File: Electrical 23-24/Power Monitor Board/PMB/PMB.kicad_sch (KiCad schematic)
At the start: 11 parts, among them J1 Conn_01x03_Pin

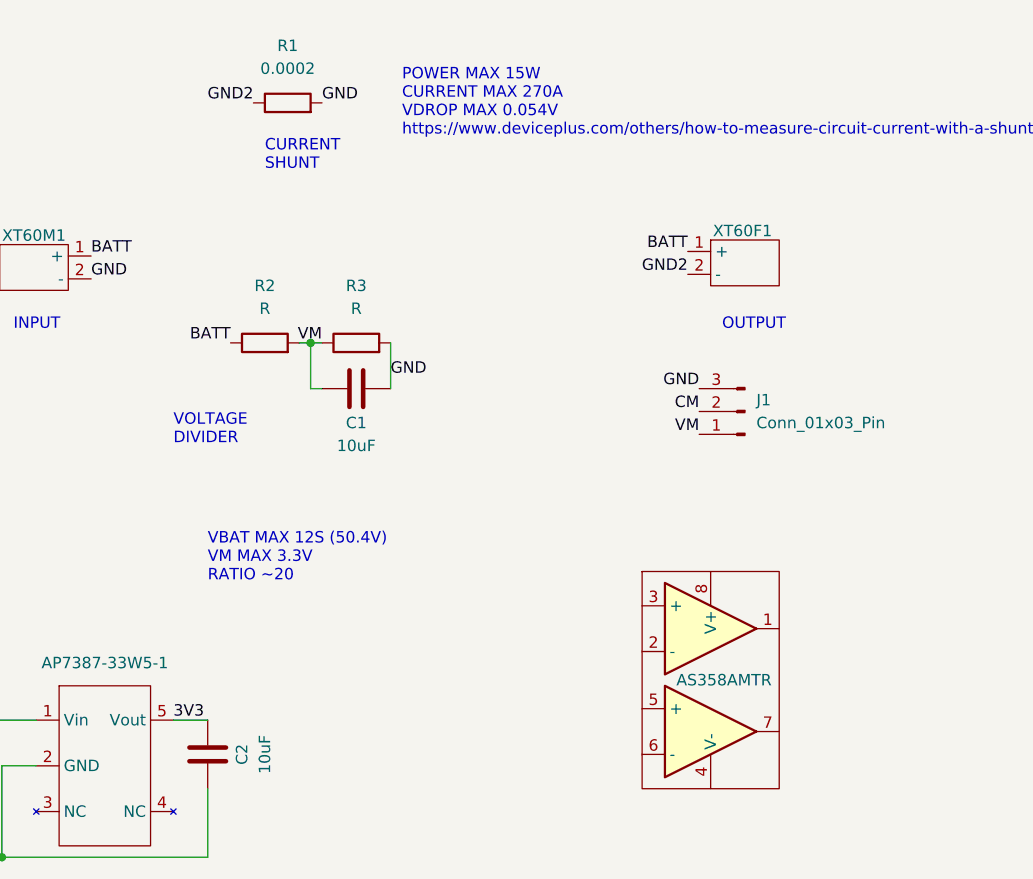
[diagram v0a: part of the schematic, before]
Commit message: Finish schematic
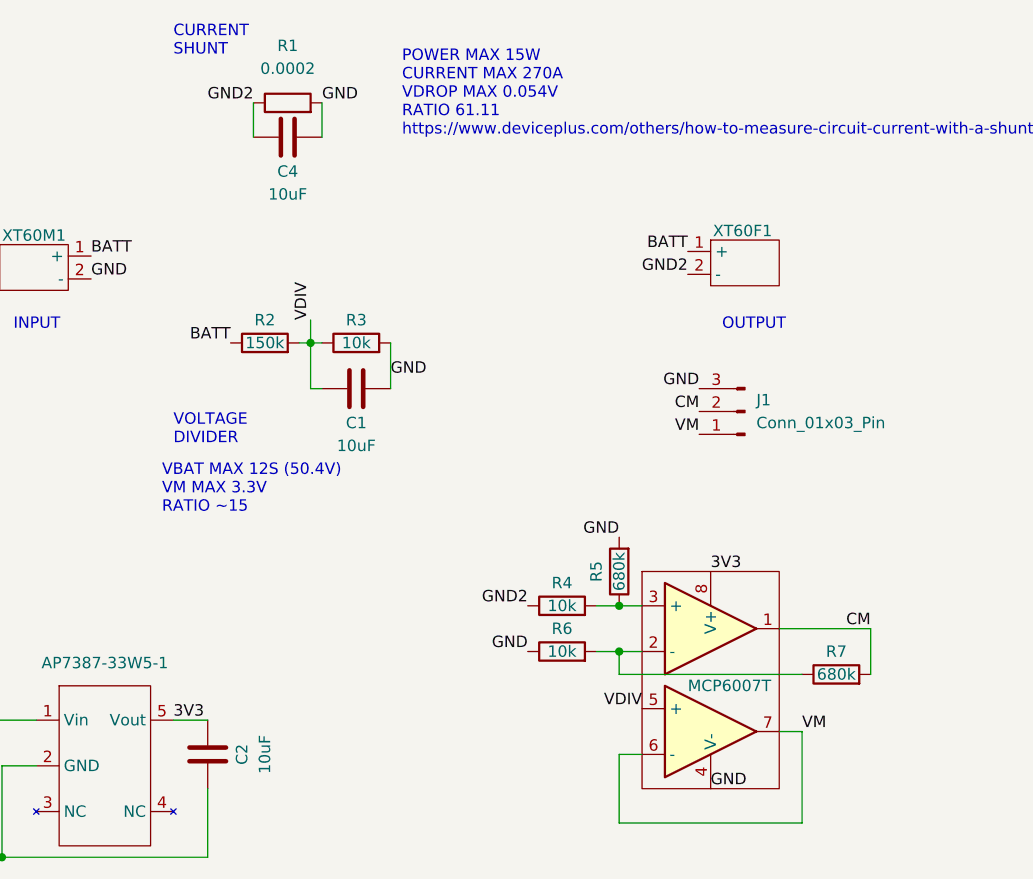
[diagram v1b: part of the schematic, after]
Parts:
- added C4: 10uF, Capacitor_SMD:C_0603_1608Metric_Pad1.08x0.95mm_HandSolder, symbol Device:C
- added R4, R6: 10k, symbol Device:R
- added R5, R7: 680k, symbol Device:R
- C1: footprint (none) -> Capacitor_SMD:C_0603_1608Metric_Pad1.08x0.95mm_HandSolder
- J1: footprint (none) -> Connector_JST:JST_XH_S3B-XH-A_1x03_P2.50mm_Horizontal
- MCP6007T: renamed from AS358AMTR; symbol PMB:AS358 -> PMB:MCP6007T-E/MS; Digi (none) -> https://www.digikey.com/en/products/detail/microchip-techno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; Num (none) -> MCP6007T-E/MS
- R1: footprint (none) -> PMB:6030_15075Metric_Pad4.20x7.60mm_HandSolder
- R2: value R -> 150k; footprint (none) -> Resistor_SMD:R_0603_1608Metric_Pad0.98x0.95mm_HandSolder
- R3: value R -> 10k; footprint (none) -> Resistor_SMD:R_0603_1608Metric_Pad0.98x0.95mm_HandSolder
- XT60F1: footprint (none) -> Connector_AMASS:AMASS_XT60PW-F_1x02_P7.20mm_Horizontal
- XT60M1: footprint (none) -> Connector_AMASS:AMASS_XT60PW-M_1x02_P7.20mm_Horizontal
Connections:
- net 3V3: now also MCP6007T.8 (V+)
- net CM: now also MCP6007T.1, R7.2
- net GND: now also MCP6007T.4 (V-), C4.2, R5.2, R6.1
- net GND2: now also C4.1, R4.1
- net VM: now also MCP6007T.6 (-), MCP6007T.7; no longer C1.1, R2.2, R3.1
- net at MCP6007T.2 (-): now also R6.2, R7.1
- net at MCP6007T.3 (+): now also R4.2, R5.1
- net VDIV: now reaches MCP6007T.5 (+)
- net VDIV: now also C1.1, R2.2, R3.1
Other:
- note added: "POWER MAX 15W CURRENT MAX 270A VDROP MAX 0.054V RATIO 61.11 https://www.deviceplus.com/others/how-to-measure-circuit-current-with-a-shunt-resistor/"
- note added: "VBAT MAX 12S (50.4V) VM MAX 3.3V RATIO ~15"
- note removed: "POWER MAX 15W CURRENT MAX 270A VDROP MAX 0.054V https://www.deviceplus.com/others/how-to-measure-circuit-current-with-a-shunt-resistor/"
- note removed: "VBAT MAX 12S (50.4V) VM MAX 3.3V RATIO ~20"

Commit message: Add all footprints
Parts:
- AP7387-33W5-1: footprint (none) -> Package_TO_SOT_SMD:SOT-23-5_HandSoldering
- C2, C3: footprint (none) -> Capacitor_SMD:C_0603_1608Metric_Pad1.08x0.95mm_HandSolder
- MCP6007T: footprint (none) -> Package_SO:TSSOP-8_4.4x3mm_P0.65mm
- R4, R5, R6, R7: footprint (none) -> Resistor_SMD:R_0603_1608Metric_Pad0.98x0.95mm_HandSolder
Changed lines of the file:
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@@
       (effects (font (size 1.27 1.27)))
     )
-    (property "Footprint" "" (at 149.86 121.92 0)
+    (property "Footprint" "Package_SO:TSSOP-8_4.4x3mm_P0.65mm" (at 149.86 121.92 0)
       (effects (font (size 1.27 1.27)) hide)
     )
@@
       (effects (font (size 1.27 1.27)))
     )
-    (property "Footprint" "" (at 94.2848 132.08 0)
+    (property "Footprint" "Capacitor_SMD:C_0603_1608Metric_Pad1.08x0.95mm_HandSolder" (at 94.2848 132.08 0)
       (effects (font (size 1.27 1.27)) hide)
     )
@@
       (effects (font (size 1.27 1.27)))
     )
-    (property "Footprint" "" (at 142.748 115.57 90)
+    (property "Footprint" "Resistor_SMD:R_0603_1608Metric_Pad0.98x0.95mm_HandSolder" (at 142.748 115.57 90)
       (effects (font (size 1.27 1.27)) hide)
     )
@@
       (effects (font (size 1.27 1.27)))
     )
-    (property "Footprint" "" (at 134.62 126.238 90)
+    (property "Footprint" "Resistor_SMD:R_0603_1608Metric_Pad0.98x0.95mm_HandSolder" (at 134.62 126.238 90)
       (effects (font (size 1.27 1.27)) hide)
     )
@@
       (effects (font (size 1.27 1.27)))
     )
-    (property "Footprint" "" (at 165.1 128.778 90)
+    (property "Footprint" "Resistor_SMD:R_0603_1608Metric_Pad0.98x0.95mm_HandSolder" (at 165.1 128.778 90)
       (effects (font (size 1.27 1.27)) hide)
     )
@@
       (effects (font (size 1.27 1.27)))
     )
-    (property "Footprint" "" (at 68.2752 139.7 0)
+    (property "Footprint" "Capacitor_SMD:C_0603_1608Metric_Pad1.08x0.95mm_HandSolder" (at 68.2752 139.7 0)
       (effects (font (size 1.27 1.27)) hide)
     )
@@
       (effects (font (size 1.27 1.27)))
     )
-    (property "Footprint" "" (at 83.82 137.16 0)
+    (property "Footprint" "Package_TO_SOT_SMD:SOT-23-5_HandSoldering" (at 83.82 137.16 0)
       (effects (font (size 1.27 1.27)) hide)
     )
@@
       (effects (font (size 1.27 1.27)))
     )
-    (property "Footprint" "" (at 134.62 121.158 90)
-      (effects (font (size 1.27 1.27)) hide)
-    )
+    (property "Footprint" "Resistor_SMD:R_0603_1608Metric_Pad0.98x0.95mm_HandSolder" (at 134.62 121.158 90)
+      (effects (font (size 1.27 1.27)) hide)
+    )

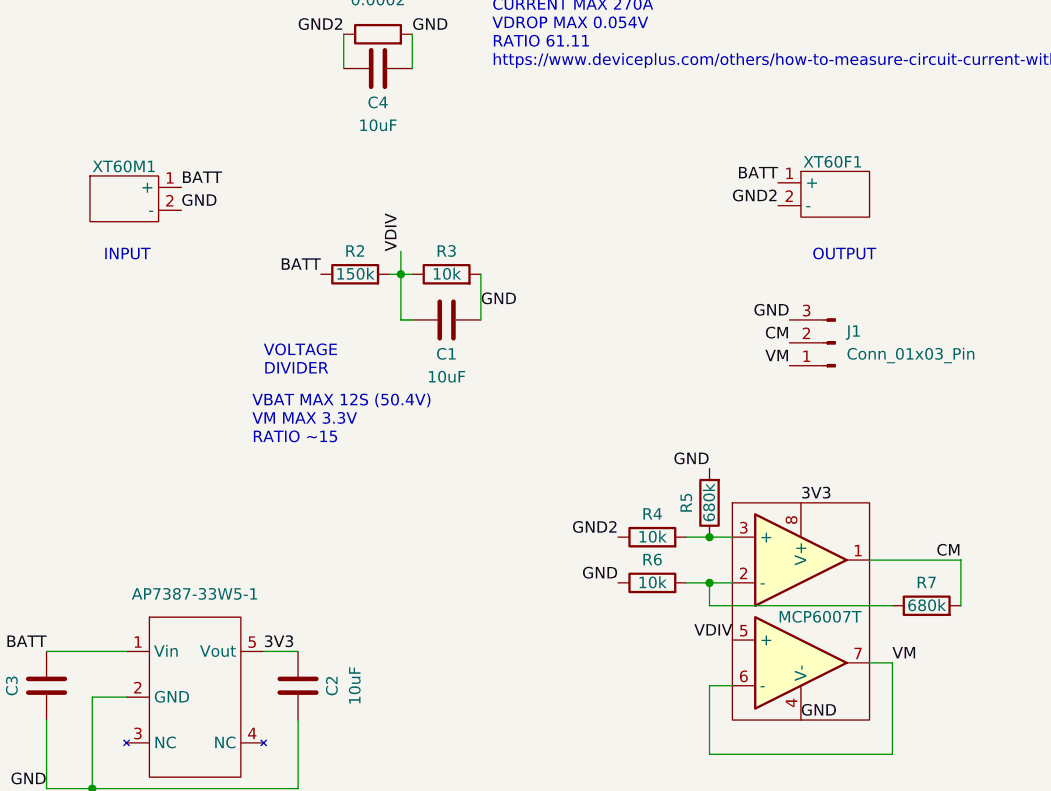
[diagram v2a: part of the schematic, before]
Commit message: Started layout
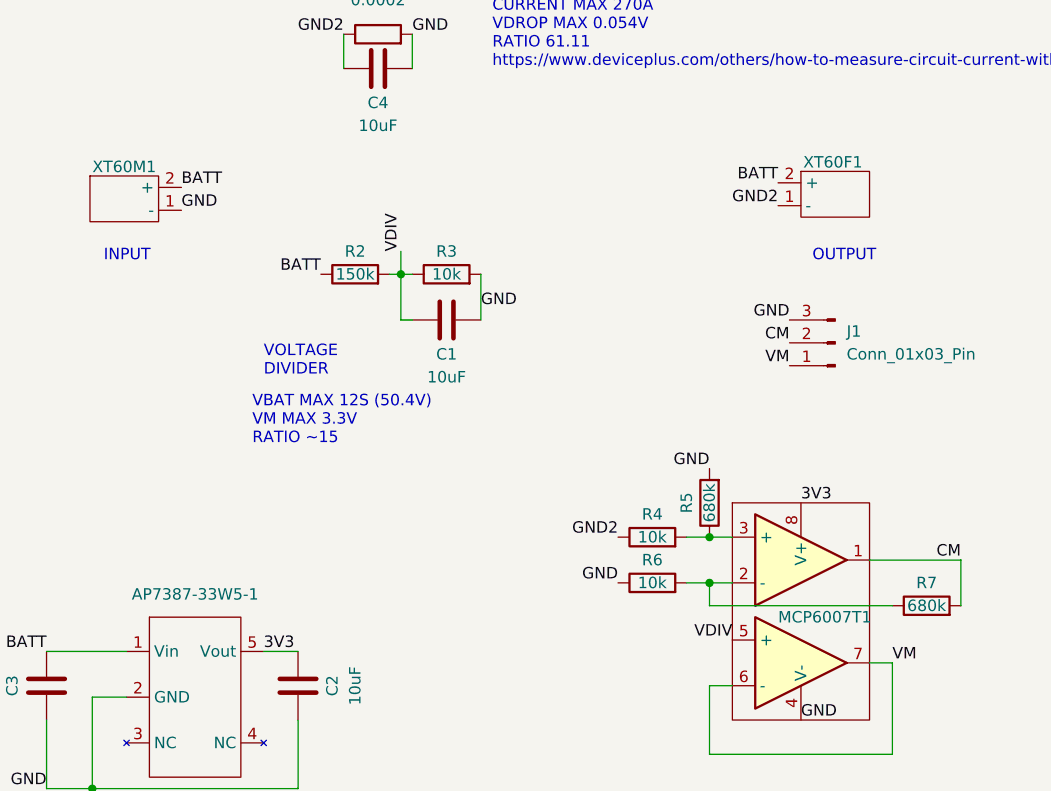
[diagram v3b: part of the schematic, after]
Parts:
- MCP6007T1: renamed from MCP6007T; footprint Package_SO:TSSOP-8_4.4x3mm_P0.65mm -> Package_SO:TSSOP-8_3x3mm_P0.65mm
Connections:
- net BATT: now also XT60F1.2 (+), XT60M1.2 (+); no longer XT60F1.1 (+), XT60M1.1 (+)
- net GND: now also XT60M1.1 (-); no longer XT60M1.2 (-)
- net GND2: now also XT60F1.1 (-); no longer XT60F1.2 (-)
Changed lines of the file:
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@@
   (symbol (lib_id "PMB:MCP6007T-E/MS") (at 149.86 121.92 0) (unit 1)
     (in_bom yes) (on_board yes) (dnp no)
-    (property "Reference" "MCP6007T" (at 148.59 128.27 0)
+    (property "Reference" "MCP6007T1" (at 148.59 128.27 0)
       (effects (font (size 1.27 1.27)) (justify left))
     )
@@
       (effects (font (size 1.27 1.27)))
     )
-    (property "Footprint" "Package_SO:TSSOP-8_4.4x3mm_P0.65mm" (at 149.86 121.92 0)
+    (property "Footprint" "Package_SO:TSSOP-8_3x3mm_P0.65mm" (at 149.86 121.92 0)
       (effects (font (size 1.27 1.27)) hide)
     )
@@
       (project "PMB"
         (path "/9d1f1551-ce55-43c8-b593-2802df254ad7"
-          (reference "MCP6007T") (unit 1)
+          (reference "MCP6007T1") (unit 1)
         )
       )

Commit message: Finish PMB
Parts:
- BATT1: renamed from XT60M1; footprint Connector_AMASS:AMASS_XT60PW-M_1x02_P7.20mm_Horizontal -> PMB:Power; symbol PMB:XT60M -> Connector:Conn_01x02_Pin
- OUT1: renamed from XT60F1; footprint Connector_AMASS:AMASS_XT60PW-F_1x02_P7.20mm_Horizontal -> PMB:Power; symbol PMB:XT60F -> Connector:Conn_01x02_Pin
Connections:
- net BATT: now also OUT1.1 (Pin_1); no longer OUT1.2 (+)
- net GND2: now also OUT1.2 (Pin_2); no longer OUT1.1 (-)
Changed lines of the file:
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@@
     (effects (font (size 1.27 1.27)) (justify right bottom))
+  )
+  (label "GND" (at 78.74 81.28 0) (fields_autoplaced)
+    (effects (font (size 1.27 1.27)) (justify left bottom))
   )
   (label "VDIV" (at 106.68 87.63 90) (fields_autoplaced)
@@
     (effects (font (size 1.27 1.27)) (justify right bottom))
   )
-  (label "GND2" (at 148.59 82.55 180) (fields_autoplaced)
+  (label "GND2" (at 152.4 83.82 180) (fields_autoplaced)
     (effects (font (size 1.27 1.27)) (justify right bottom))
   )
@@
     (effects (font (size 1.27 1.27)) (justify right bottom))
   )
-  (label "BATT" (at 148.59 80.01 180) (fields_autoplaced)
-    (effects (font (size 1.27 1.27)) (justify right bottom))
+  (label "BATT" (at 152.4 81.28 180) (fields_autoplaced)
+    (effects (font (size 1.27 1.27)) (justify right bottom))
+  )
+  (label "BATT" (at 78.74 83.82 0) (fields_autoplaced)
+    (effects (font (size 1.27 1.27)) (justify left bottom))
   )
   (label "VDIV" (at 143.51 130.81 180) (fields_autoplaced)
@@
     (effects (font (size 1.27 1.27)) (justify right bottom))
   )
-  (label "GND" (at 82.296 83.058 0) (fields_autoplaced)
-    (effects (font (size 1.27 1.27)) (justify left bottom))
-  )
   (label "GND" (at 67.31 147.32 180) (fields_autoplaced)
     (effects (font (size 1.27 1.27)) (justify right bottom))
-  )
-  (label "BATT" (at 82.296 80.518 0) (fields_autoplaced)
-    (effects (font (size 1.27 1.27)) (justify left bottom))
   )
   (label "BATT" (at 67.31 132.08 180) (fields_autoplaced)
@@
     )
   )
-  (symbol (lib_id "PMB:XT60F") (at 154.94 81.28 0) (unit 1)
-    (in_bom yes) (on_board yes) (dnp no)
-    (property "Reference" "XT60F1" (at 151.384 77.724 0)
+  (symbol (lib_id "Connector:Conn_01x02_Pin") (at 157.48 81.28 0) (mirror y) (unit 1)
+    (in_bom yes) (on_board yes) (dnp no)
+    (property "Reference" "OUT1" (at 156.21 77.47 0)
       (effects (font (size 1.27 1.27)) (justify left))
     )
-    (property "Value" "~" (at 154.94 81.28 0)
-      (effects (font (size 1.27 1.27)))
-    )
-    (property "Footprint" "Connector_AMASS:AMASS_XT60PW-F_1x02_P7.20mm_Horizontal" (at 154.94 81.28 0)
-      (effects (font (size 1.27 1.27)) hide)
-    )
-    (property "Datasheet" "" (at 154.94 81.28 0)
-      (effects (font (size 1.27 1.27)) hide)
-    )
-    (pin "1")
-    (pin "2")
-    (instances
-      (project "PMB"
-        (path "/9d1f1551-ce55-43c8-b593-2802df254ad7"
-          (reference "XT60F1") (unit 1)
+    (property "Value" "~" (at 157.48 81.28 0)
+      (effects (font (size 1.27 1.27)))
+    )
+    (property "Footprint" "PMB:Power" (at 157.48 81.28 0)
+      (effects (font (size 1.27 1.27)) hide)
+    )
+    (property "Datasheet" "~" (at 157.48 81.28 0)
+      (effects (font (size 1.27 1.27)) hide)
+    )
+    (pin "1")
+    (pin "2")
+    (instances
+      (project "PMB"
+        (path "/9d1f1551-ce55-43c8-b593-2802df254ad7"
+          (reference "OUT1") (unit 1)
         )
       )
@@
     )
   )
-  (symbol (lib_id "PMB:XT60M") (at 75.946 81.788 0) (unit 1)
-    (in_bom yes) (on_board yes) (dnp no)
-    (property "Reference" "XT60M1" (at 75.946 78.232 0)
-      (effects (font (size 1.27 1.27)))
-    )
-    (property "Value" "XT60M" (at 75.946 81.788 0)
-      (effects (font (size 1.27 1.27)) hide)
-    )
-    (property "Footprint" "Connector_AMASS:AMASS_XT60PW-M_1x02_P7.20mm_Horizontal" (at 75.946 81.788 0)
-      (effects (font (size 1.27 1.27)) hide)
-    )
-    (property "Datasheet" "" (at 75.946 81.788 0)
-      (effects (font (size 1.27 1.27)) hide)
-    )
-    (pin "1")
-    (pin "2")
-    (instances
-      (project "PMB"
-        (path "/9d1f1551-ce55-43c8-b593-2802df254ad7"
-          (reference "XT60M1") (unit 1)
-        )
-      )
+  (symbol (lib_id "Connector:Conn_01x02_Pin") (at 73.66 81.28 0) (unit 1)
+    (in_bom yes) (on_board yes) (dnp no)
+    (property "Reference" "BATT1" (at 76.2 77.47 0)
+      (effects (font (size 1.27 1.27)))
+    )
+    (property "Value" "XT60M" (at 73.66 81.28 0)
+      (effects (font (size 1.27 1.27)) hide)
+    )
+    (property "Footprint" "PMB:Power" (at 73.66 81.28 0)
+      (effects (font (size 1.27 1.27)) hide)
+    )
+    (property "Datasheet" "~" (at 73.66 81.28 0)
+      (effects (font (size 1.27 1.27)) hide)
+    )
+    (pin "1")
+    (pin "2")
+    (instances
+      (project "PMB"
+        (path "/9d1f1551-ce55-43c8-b593-2802df254ad7"
+          (reference "BATT1") (unit 1)
+        )
+      )

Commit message: Update PMB.kicad_sch
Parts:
- BATT1: value XT60M -> 10AWG_1x02
- J1: value Conn_01x03_Pin -> JST_XH_03
- OUT1: value ~ -> 10AWG_1x02
- R2: value 150k -> 180k
- R5, R7: value 680k -> 620k
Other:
- note added: "A1 = 62 = CM/(GND2-GND) A2 = 1 = VM/VDIV"
- note added: "AMPLIFIERS"
- note added: "BATT: 0-60V (0-12S) GND2: System GND"
- note added: "BATT: 0-60V (0-12S) GND: LiPo GND"
- note added: "GND: LiPo GND GND2: System GND"
- note added: "I_max = 270A = sqrt(P_max/R) V_max = 0.054V = R*I_max Gain = 61.11 = 3.3V/V_max https://www.deviceplus.com/others/how-to-measure-circuit-current-with-a-shunt-resistor/"
- note added: "Power Monitor Board"
- note added: "Requirements: - 240A Continuous Current - Low Power Consumption - V_max < 3.3V Ratings: R = 0.0002 Ω P_max = 15W"
- note added: "VM: 0-3.3V to ADC - Voltage Meas. CM: 0-3.3V to ADC - Current Meas. GND: Common GND"
- note added: "VOLTAGE REGULATOR"
- note added: "V_max = 60V (~12S) VM_max = 3.3V Gain = 1 Ratio = 18 = Gain*V_max/VM_max"
- note added: "https://eepower.com/resistor-guide/resistor-standards-and-codes/resistor-values/"
- note removed: "POWER MAX 15W CURRENT MAX 270A VDROP MAX 0.054V RATIO 61.11 https://www.deviceplus.com/others/how-to-measure-circuit-current-with-a-shunt-resistor/"
- note removed: "VBAT MAX 12S (50.4V) VM MAX 3.3V RATIO ~15"
- moved on the sheet: AP7387-33W5-1, BATT1, C1, C2, C3, C4, J1, MCP6007T1, OUT1, R1, R2, R3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

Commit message: Final PMB
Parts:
- removed C4: 10uF, Capacitor_SMD:C_0603_1608Metric_Pad1.08x0.95mm_HandSolder, symbol Device:C
- J1: value JST_XH_03 -> JST_XH_04; footprint Connector_JST:JST_XH_S3B-XH-A_1x03_P2.50mm_Horizontal -> Connector_JST:JST_XH_S4B-XH-A_1x04_P2.50mm_Horizontal; symbol Connector:Conn_01x03_Pin -> Connector:Conn_01x04_Pin
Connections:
- net CM: now also J1.3 (Pin_3); no longer J1.2 (Pin_2)
- net GND: now also J1.2 (Pin_2), J1.4 (Pin_4); no longer J1.3 (Pin_3)
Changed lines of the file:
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@@
-    (stroke (width 0) (type default))
-  )
-  (wire (pts (xy 109.22 50.8) (xy 109.22 54.61))
     (stroke (width 0) (type default))
   )
@@
   )
   (wire (pts (xy 101.6 158.75) (xy 107.95 158.75))
-    (stroke (width 0) (type default))
-  )
-  (wire (pts (xy 101.6 50.8) (xy 101.6 54.61))
     (stroke (width 0) (type default))
   )
@@
     (effects (font (size 1.27 1.27)) (justify left bottom))
   )
-  (label "CM" (at 231.14 118.11 180) (fields_autoplaced)
-    (effects (font (size 1.27 1.27)) (justify right bottom))
-  )
   (label "GND" (at 55.88 96.52 0) (fields_autoplaced)
     (effects (font (size 1.27 1.27)) (justify left bottom))
@@
     (effects (font (size 1.27 1.27)) (justify left bottom))
   )
+  (label "GND" (at 231.14 118.11 180) (fields_autoplaced)
+    (effects (font (size 1.27 1.27)) (justify right bottom))
+  )
   (label "CM" (at 152.4 148.59 180) (fields_autoplaced)
     (effects (font (size 1.27 1.27)) (justify right bottom))
@@
     (effects (font (size 1.27 1.27)) (justify right bottom))
   )
+  (label "CM" (at 231.14 115.57 180) (fields_autoplaced)
+    (effects (font (size 1.27 1.27)) (justify right bottom))
+  )
   (label "BATT" (at 55.88 99.06 0) (fields_autoplaced)
     (effects (font (size 1.27 1.27)) (justify left bottom))
@@
     (effects (font (size 1.27 1.27)) (justify right bottom))
   )
-  (label "GND" (at 231.14 115.57 180) (fields_autoplaced)
+  (label "GND" (at 231.14 113.03 180) (fields_autoplaced)
     (effects (font (size 1.27 1.27)) (justify right bottom))
   )
@@
     )
   )
-  (symbol (lib_id "Device:C") (at 105.41 54.61 90) (unit 1)
-    (in_bom yes) (on_board yes) (dnp no)
-    (property "Reference" "C4" (at 105.41 58.42 90)
-      (effects (font (size 1.27 1.27)))
-    )
-    (property "Value" "10uF" (at 105.41 60.96 90)
-      (effects (font (size 1.27 1.27)))
-    )
-    (property "Footprint" "Capacitor_SMD:C_0603_1608Metric_Pad1.08x0.95mm_HandSolder" (at 109.22 53.6448 0)
-      (effects (font (size 1.27 1.27)) hide)
-    )
-    (property "Datasheet" "~" (at 105.41 54.61 0)
-      (effects (font (size 1.27 1.27)) hide)
-    )
-    (pin "1")
-    (pin "2")
-    (instances
-      (project "PMB"
-        (path "/9d1f1551-ce55-43c8-b593-2802df254ad7"
-          (reference "C4") (unit 1)
-        )
-      )
-    )
-  )
   (symbol (lib_id "Device:R") (at 107.95 154.94 180) (unit 1)
     (in_bom yes) (on_board yes) (dnp no)
@@
     )
   )
-  (symbol (lib_id "Connector:Conn_01x03_Pin") (at 236.22 118.11 180) (unit 1)
+  (symbol (lib_id "Connector:Conn_01x04_Pin") (at 236.22 118.11 180) (unit 1)
     (in_bom yes) (on_board yes) (dnp no) (fields_autoplaced)
-    (property "Reference" "J1" (at 237.49 116.84 0)
+    (property "Reference" "J1" (at 237.49 115.57 0)
       (effects (font (size 1.27 1.27)) (justify right))
     )
-    (property "Value" "JST_XH_03" (at 237.49 119.38 0)
+    (property "Value" "JST_XH_04" (at 237.49 118.11 0)
       (effects (font (size 1.27 1.27)) (justify right))
     )
-    (property "Footprint" "Connector_JST:JST_XH_S3B-XH-A_1x03_P2.50mm_Horizontal" (at 236.22 118.11 0)
+    (property "Footprint" "Connector_JST:JST_XH_S4B-XH-A_1x04_P2.50mm_Horizontal" (at 236.22 118.11 0)
       (effects (font (size 1.27 1.27)) hide)
     )
@@
     (pin "2")
     (pin "3")
-    (instances
-      (project "PMB"
+    (pin "4")
+    (instances
+      (project "PMB"
